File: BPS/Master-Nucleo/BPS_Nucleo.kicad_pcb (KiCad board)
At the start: 2 copper layers, 69.8 x 113 mm, 115 parts, among them J1 ContactorConnector, J11 CAN_Out, J12 Conn_01x04, J2 CarPowerConnector, J3 Conn_01x03, J4 FrontFans, J5 ErrorLightConnector, J6 BackFans, J7 VoltageSlaveConnector, Q1 VND5N07-E, Q2 NTR4003NT1G, Q3 NTR4003NT1G, Q4 NTR4003NT1G, U1 NUCLEO144-F412ZG, U14 ADM3055E, U2 BAS70-04, U3 SI8261ABC-IS, U4 RI3-1205S, U5 CDSOT23-T24CAN, U6 M24128, U7 SI8261ABC-IS, U8 LTC6820, U9 HX1188FNL

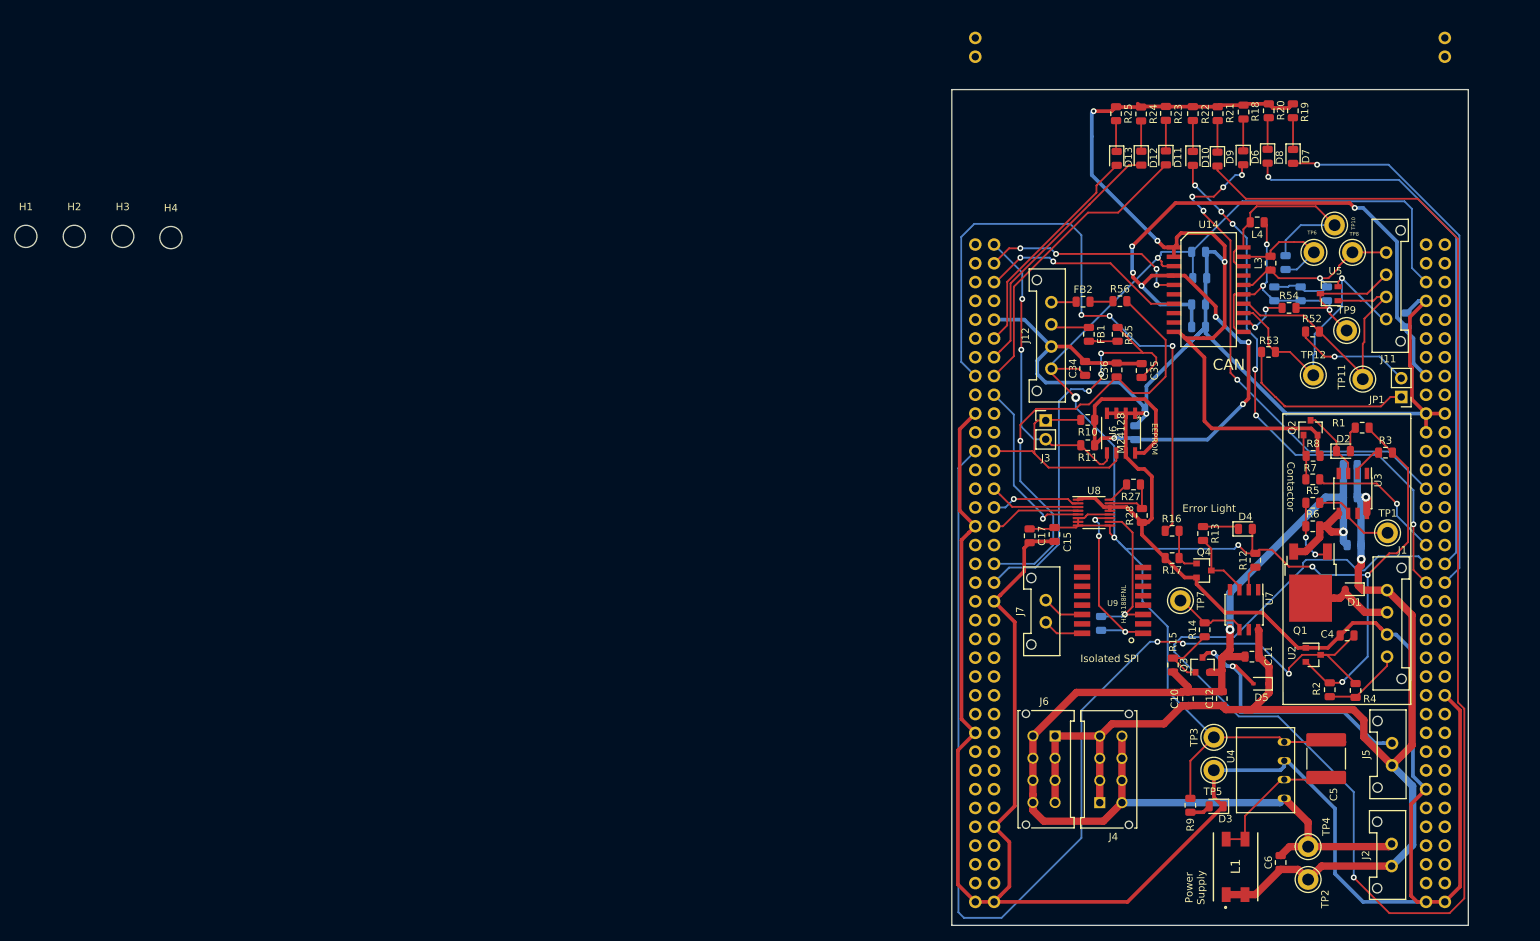
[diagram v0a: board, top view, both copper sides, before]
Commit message: Added silkscreens to certain diodes and testpoints
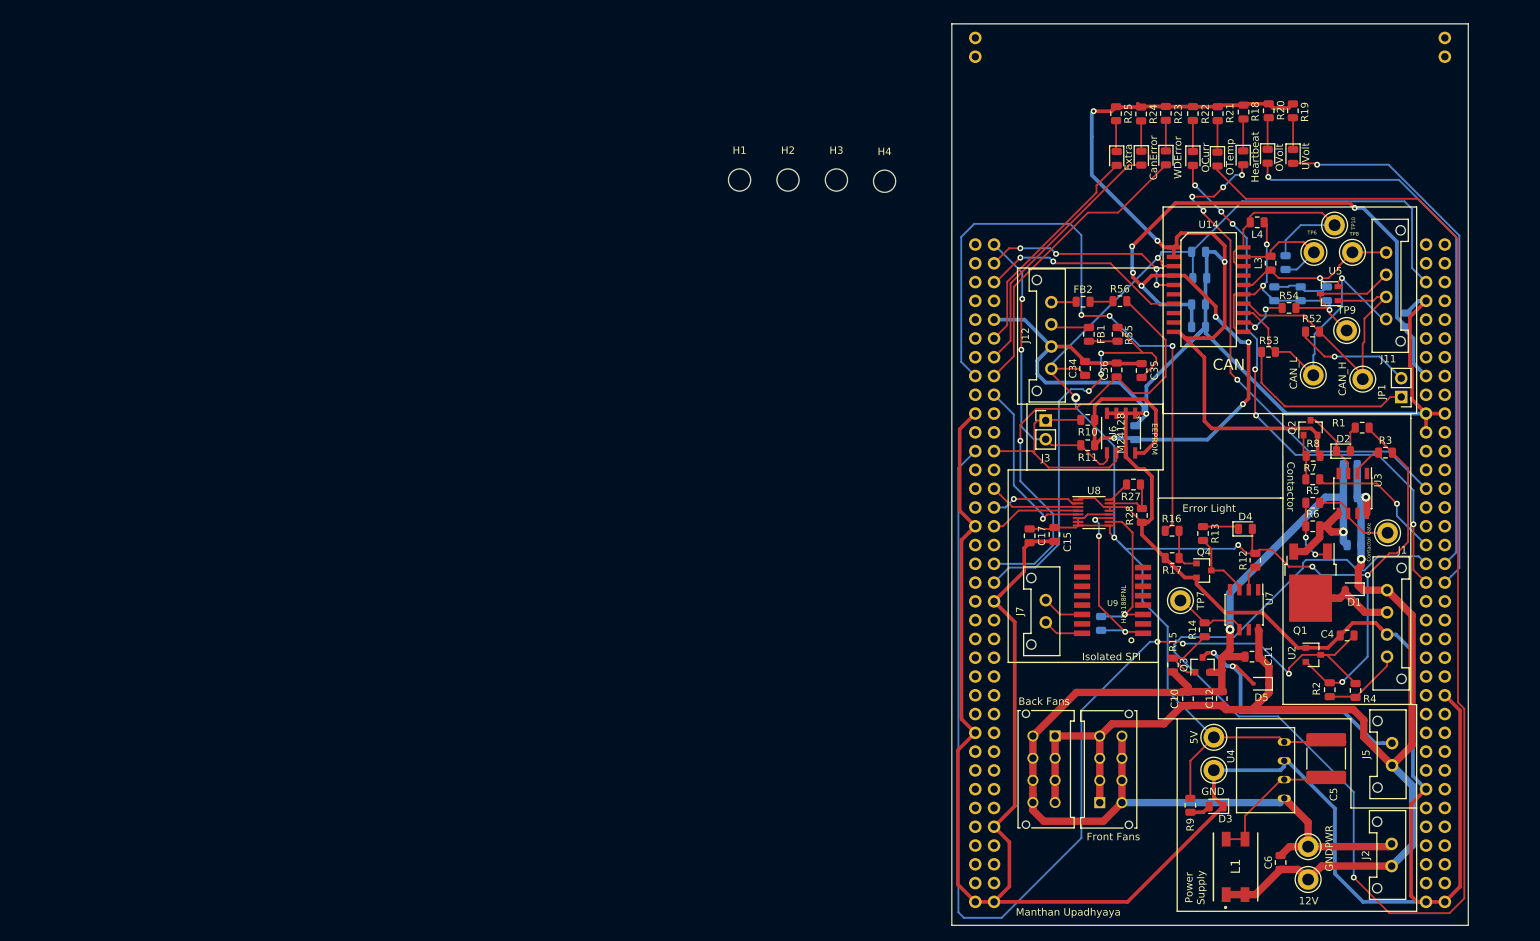
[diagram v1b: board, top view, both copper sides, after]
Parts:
- removed TP12: CAN_L, TestPoint:TestPoint_Keystone_5005-5009_Compact
- added CAN_L: CAN_L, TestPoint:TestPoint_Keystone_5005-5009_Compact, F.Cu at (219.1, 76.7)
- Back Fans: renamed from J6
- Contactor Gate: renamed from TP1
- Front Fans: renamed from J4
- moved H2 96.8 mm to (148.0, 50.3)
- moved H3 96.8 mm to (154.6, 50.3)
- moved H4 96.8 mm to (161.1, 50.5)
- moved H1 96.8 mm to (141.5, 50.3)
- renumbered TP2 to 12V, TP3 to 5V, TP11 to CAN_H, D12 to CanError, D13 to Extra, TP5 to GND, TP4 to GNDPWR, D6 to Heartbeat, D10 to OCurr, D9 to OTemp, D8 to OVolt, D7 to UVolt, D11 to WDError
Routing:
- net Net-(C8-Pad2): track 31.8 -> 30.8 mm
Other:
- board size 69.8 x 113 mm -> 69.8 x 121.9 mm
- rule trace_min: 0.1 -> 0.127
- board text added: "Manthan Upadhyaya"

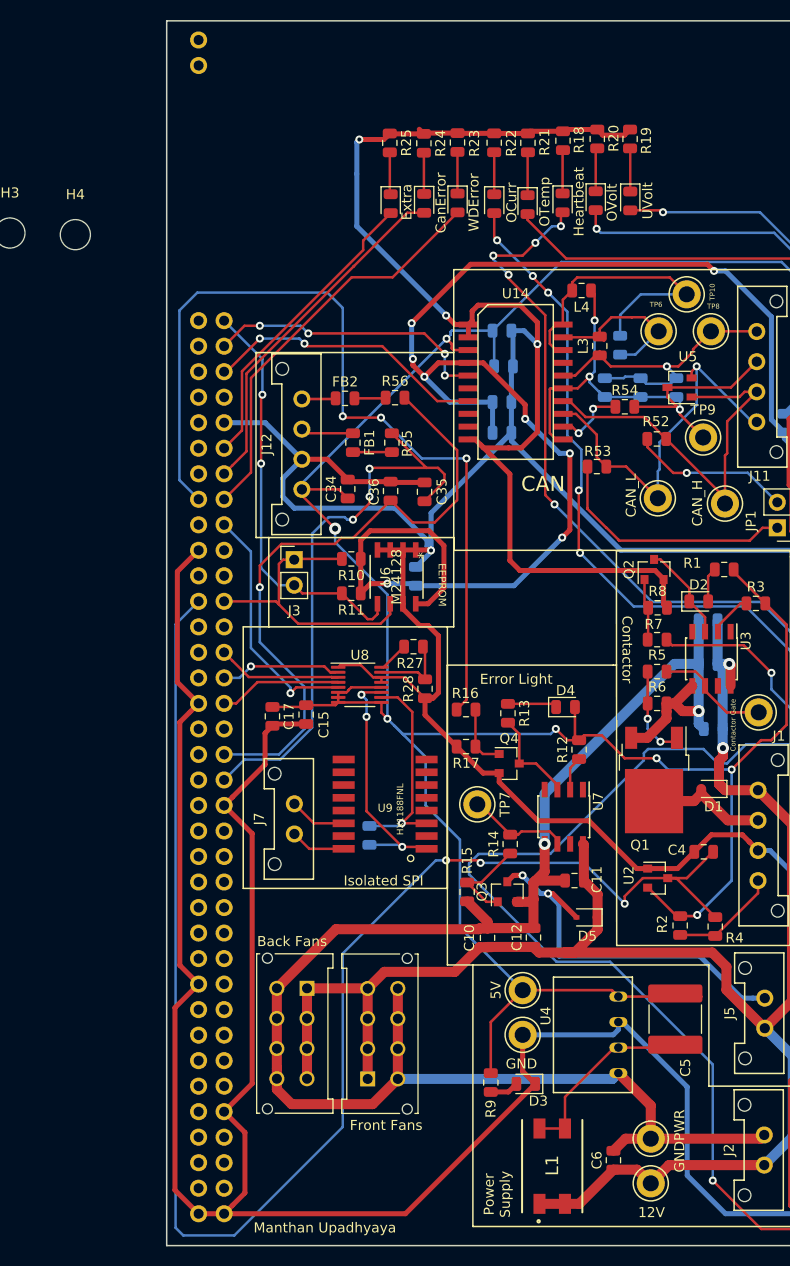
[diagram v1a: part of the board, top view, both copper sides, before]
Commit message: Increased area of PCB to include upper components. Added silkscreen of Dr. Hallock.
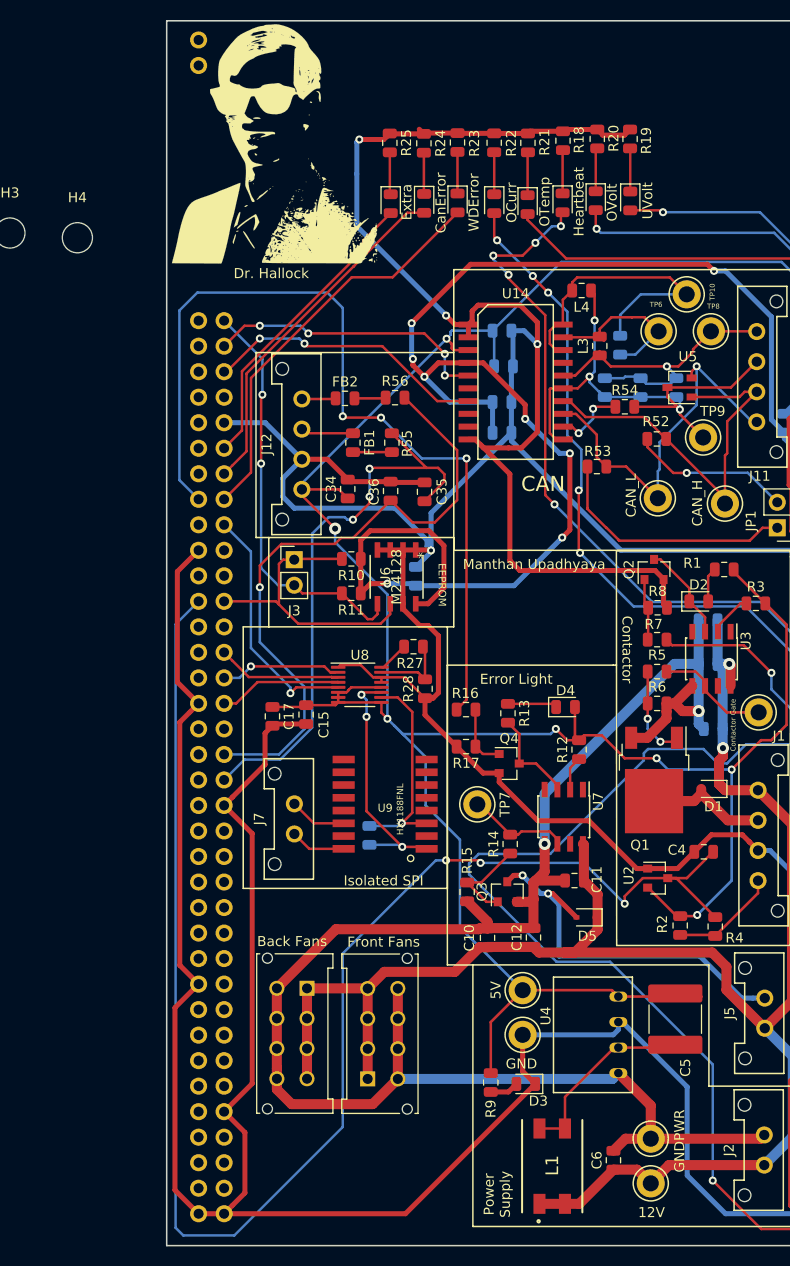
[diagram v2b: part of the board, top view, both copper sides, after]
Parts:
- added G***: LOGO, UTSVT_Special:Hallock_Image_Small, F.Cu at (180.1, 41.1)
- moved H4 0.37 mm to (161.3, 50.8)
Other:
- board text added: "Dr. Hallock"

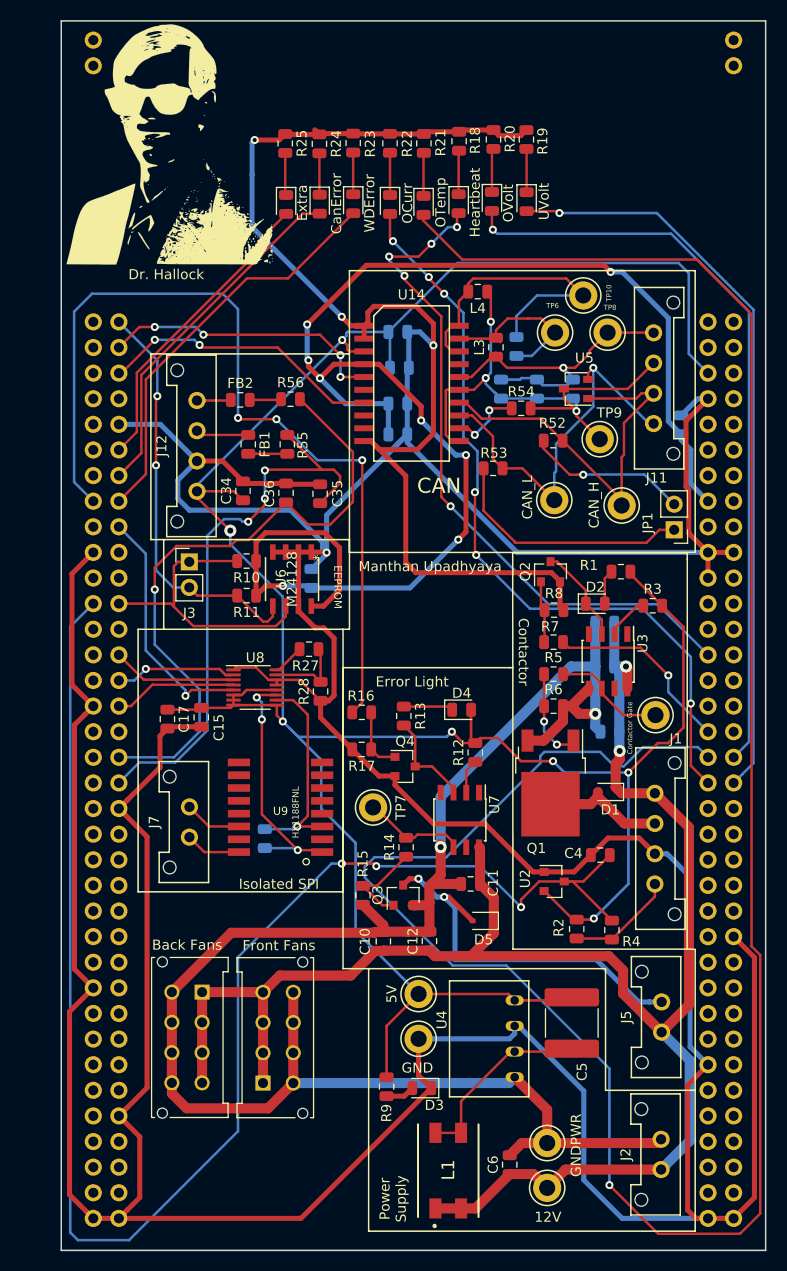
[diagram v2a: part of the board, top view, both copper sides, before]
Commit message: Decreased length of PCB on top, left, and bottom and spaced out some resistors in the EEPROM.
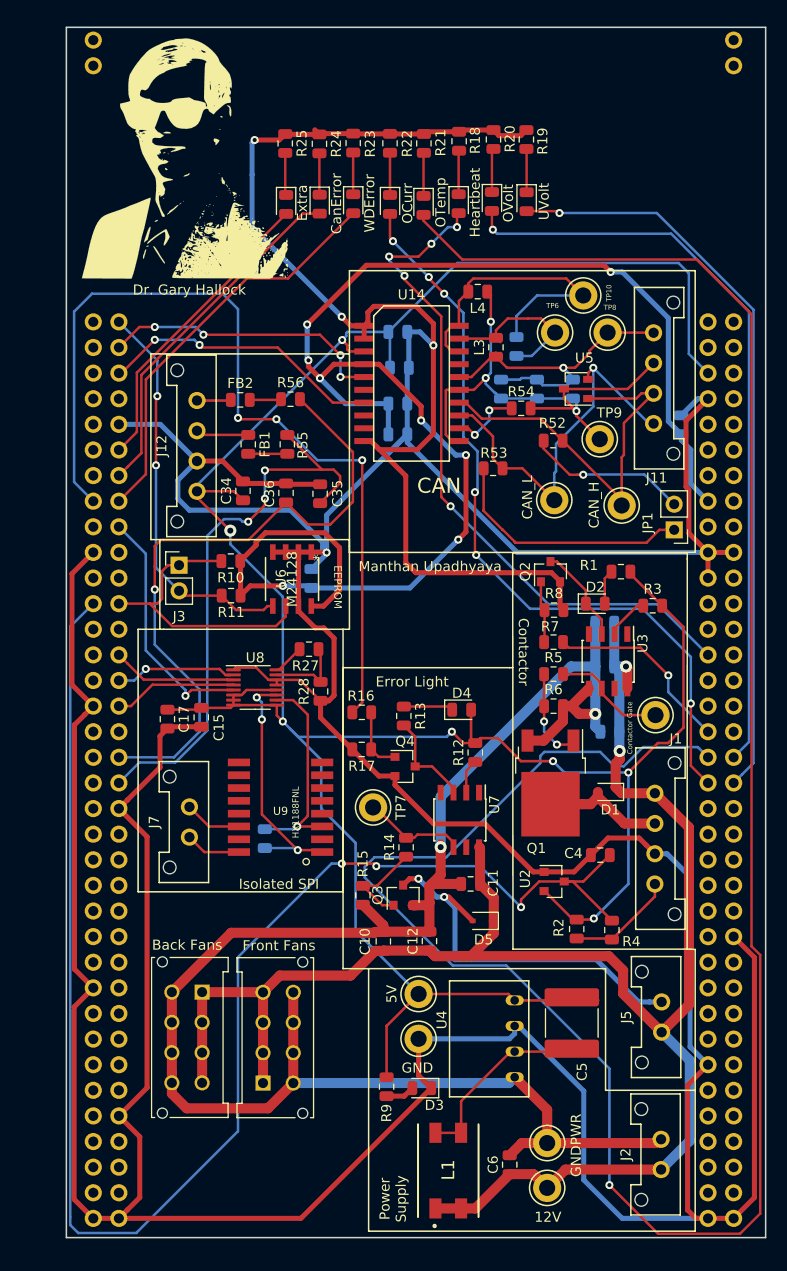
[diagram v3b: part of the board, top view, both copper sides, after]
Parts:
- moved G*** 2.07 mm to (181.6, 42.5)
- moved R10 1.57 mm to (187.0, 82.8)
- moved R11 1.54 mm to (187.0, 86.2)
- moved J3 1.07 mm to (181.9, 83.2)
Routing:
- net +3V3: track 150.7 -> 152.9 mm
- net /I2C3_SDA: track 41.2 -> 39.5 mm
- net /ADC1_CH2: track 63.7 -> 64.9 mm
- net /PB1: track 153.4 -> 152.4 mm
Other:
- board size 69.8 x 121.9 mm -> 69.3 x 120 mm
- board text added: "Dr. Gary Hallock"
- board text removed: "Dr. Hallock"

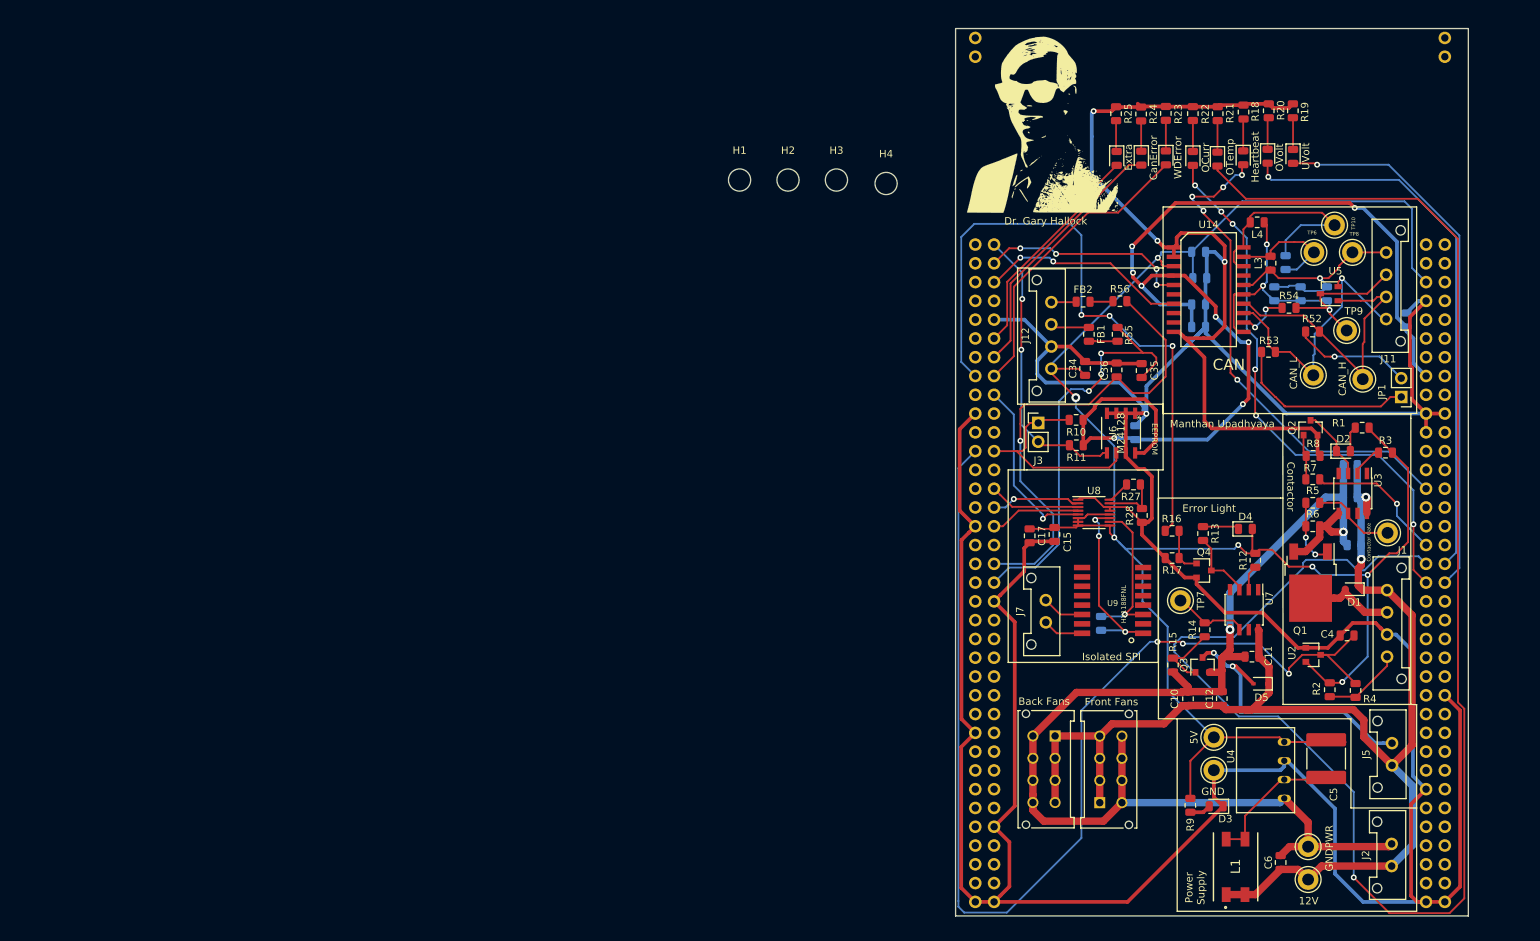
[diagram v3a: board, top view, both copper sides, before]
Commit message: Added mounting holes and footprints. Increased track length of 5v from .25 to .38.
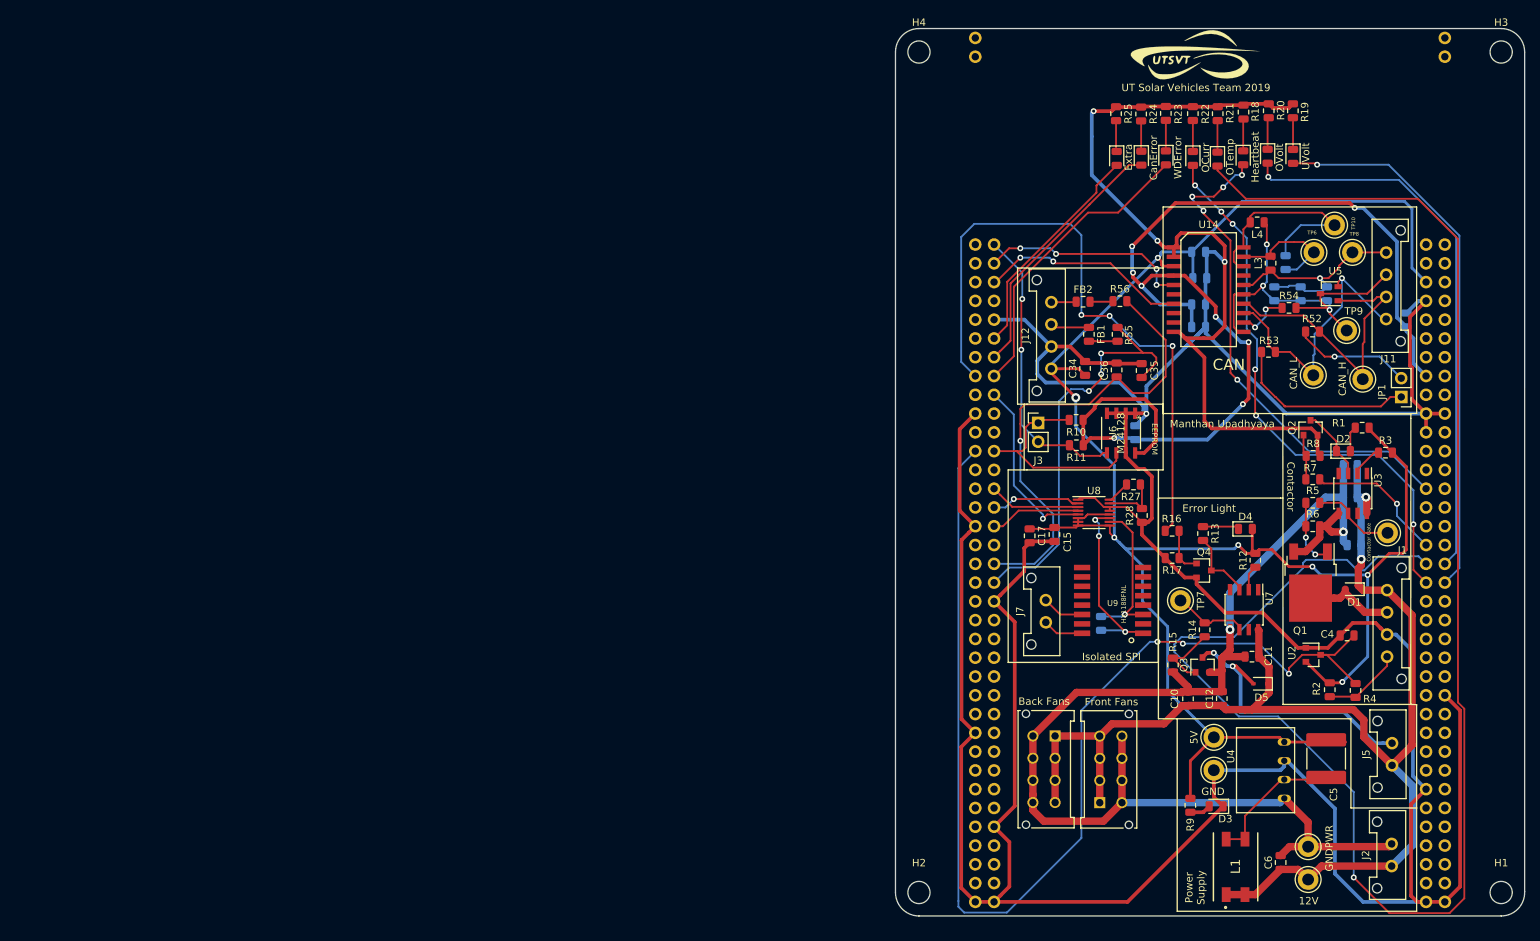
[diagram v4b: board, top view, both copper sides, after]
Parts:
- added G***: LOGO, UTSVT_Special:UTSVT_Logo_Symbol, F.Cu at (202.8, 33.5)
- G***: moved to B.Cu
- moved H1 141.0 mm to (244.5, 146.7)
- moved H2 98.0 mm to (165.7, 146.7)
- moved H3 91.6 mm to (244.5, 33.0)
- moved H4 18.3 mm to (165.7, 33.0)
- moved G*** 0.90 mm to (182.5, 42.4), turned to 180 degrees
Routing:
- net GND: track 620.7 -> 620.1 mm
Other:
- board size 69.3 x 120 mm -> 85.1 x 120 mm
- board text added: "UT Solar Vehicles Team 2019"
